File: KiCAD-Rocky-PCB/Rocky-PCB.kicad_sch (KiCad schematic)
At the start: 0 parts

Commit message: Schematic and Sym lib
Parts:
- added BT1: 3.7V Li-Po, symbol Device:Battery_Cell
- added SW1: PWR SW, symbol Switch:SW_SPST
- added U1: ESP32 S3 Sence, symbol Rocky:ESP32-S3-Sence
- added U2: BMP390, symbol Rocky:BMP390
- added U3: GY-91, symbol Rocky:GY-91
- added U4: LC76G, symbol Rocky:LC76G
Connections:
- new net: SW1.2 (B), U1.15 (B+)
- new net: BT1.2 (-), U1.16 (B-)
- new net: BT1.1 (+), SW1.1 (A)
- new net +3.3V: U1.12 (3V3), U2.1 (VCC), U4.1 (VCC)
- new net GND: U1.13 (GND), U2.2 (GND), U3.2 (GND), U4.2 (GND)
- new net I2C-SCL: U1.6 (D5/SCL), U2.4 (SCL), U3.4 (SCL)
- new net I2C-SDA: U1.5 (D4/SDA), U2.3 (SDA), U3.3 (SDA)
- new net uC-Rx: U1.8 (D7/Rx), U4.3 (Tx)
- new net uC-Tx: U1.7 (D6/Tx), U4.4 (Rx)
- no-connect marks 0 -> 7

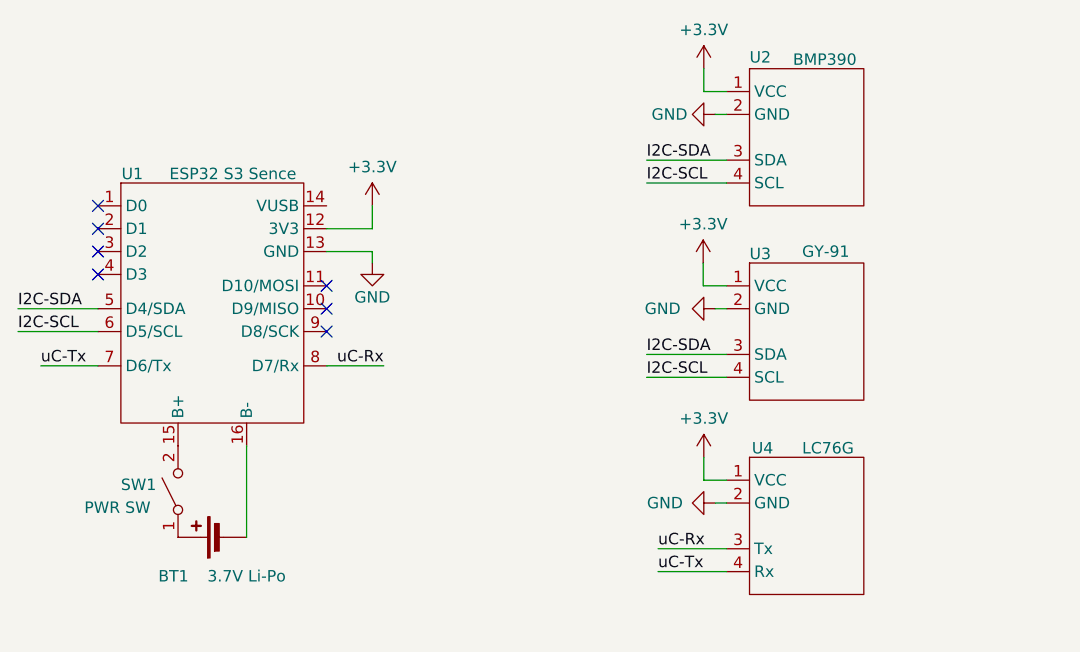
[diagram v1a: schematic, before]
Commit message: Added filtering capacitor and fixed some errors
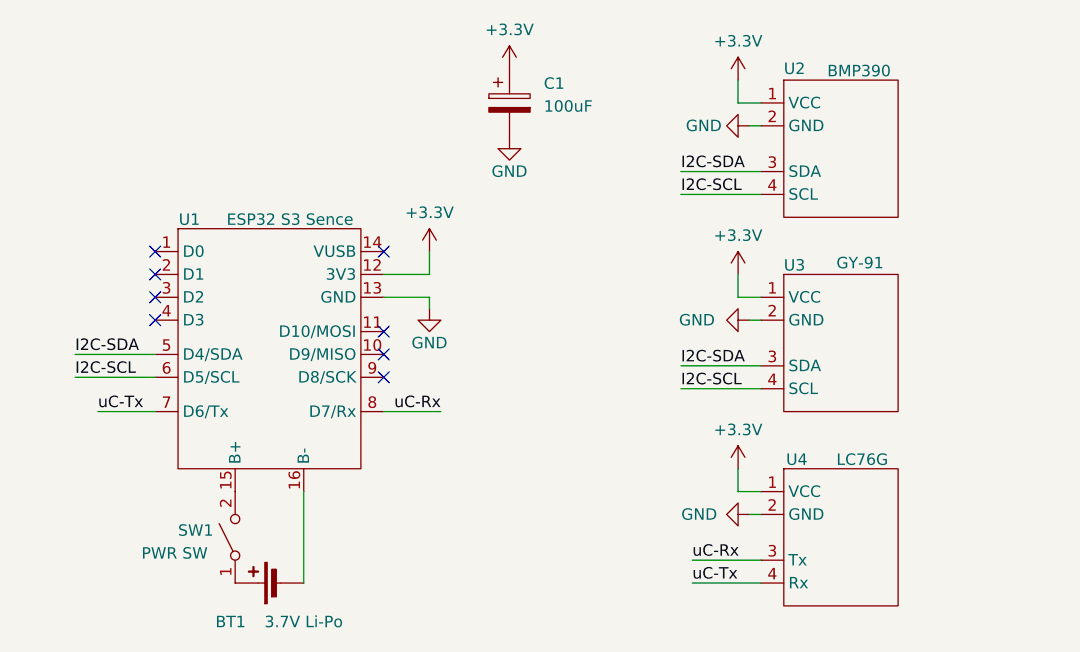
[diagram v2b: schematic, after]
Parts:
- added C1: 100uF, symbol Device:C_Polarized
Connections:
- net +3.3V: now also U3.1 (VCC), C1.1
- net GND: now also C1.2
- no-connect marks 7 -> 8
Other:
- moved on the sheet: BT1, SW1, U1, U2, U3, U4

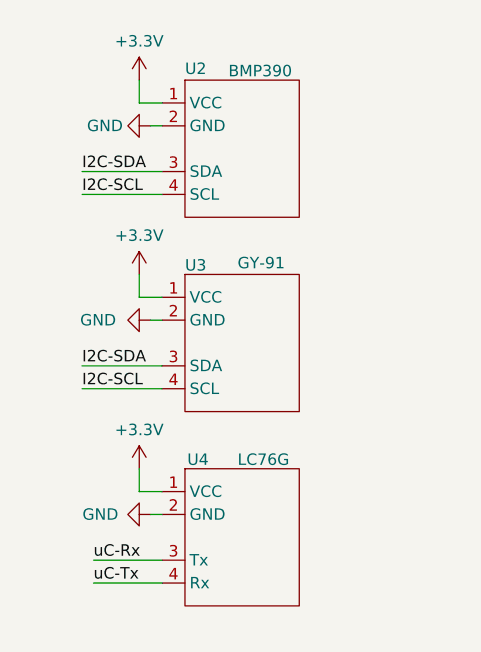
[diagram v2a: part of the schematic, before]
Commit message: Added new filtering capacitors and added a picture of the schematic
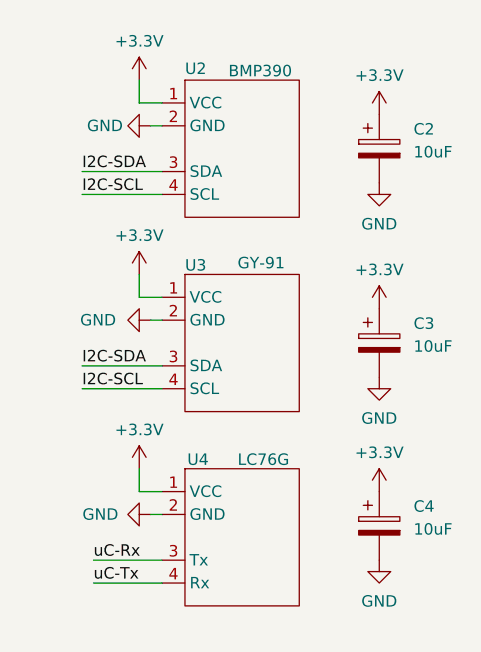
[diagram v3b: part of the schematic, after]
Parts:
- added C2, C3, C4: 10uF, symbol Device:C_Polarized
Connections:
- net +3.3V: now also C2.1, C3.1, C4.1
- net GND: now also C2.2, C3.2, C4.2

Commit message: PCB-V1
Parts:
- BT1: footprint (none) -> Connector_JST:JST_XH_B2B-XH-AM_1x02_P2.50mm_Vertical
- C1: footprint (none) -> Capacitor_THT:CP_Radial_Tantal_D5.5mm_P2.50mm
- C2, C3, C4: footprint (none) -> Capacitor_THT:CP_Radial_Tantal_D4.5mm_P2.50mm
- SW1: footprint (none) -> Rocky-Footprints:DIP4-SW
- U1: footprint (none) -> Rocky-Footprints:XIAO-ESP32-S3-Sence
- U2, U3, U4: footprint (none) -> Connector_JST:JST_XH_B4B-XH-A_1x04_P2.50mm_Vertical
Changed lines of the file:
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@@
 			)
 		)
-		(property "Footprint" ""
+		(property "Footprint" "Rocky-Footprints:XIAO-ESP32-S3-Sence"
 			(at 116.84 105.41 0)
 			(effects
@@
 			)
 		)
-		(property "Footprint" ""
+		(property "Footprint" "Capacitor_THT:CP_Radial_Tantal_D4.5mm_P2.50mm"
 			(at 196.5452 87.63 0)
 			(effects
@@
 			)
 		)
-		(property "Footprint" ""
+		(property "Footprint" "Capacitor_THT:CP_Radial_Tantal_D4.5mm_P2.50mm"
 			(at 196.5452 109.22 0)
 			(effects
@@
 			)
 		)
-		(property "Footprint" ""
+		(property "Footprint" "Connector_JST:JST_XH_B2B-XH-AM_1x02_P2.50mm_Vertical"
 			(at 116.586 132.08 90)
 			(effects
@@
 			)
 		)
-		(property "Footprint" ""
+		(property "Footprint" "Capacitor_THT:CP_Radial_Tantal_D4.5mm_P2.50mm"
 			(at 196.5452 129.54 0)
 			(effects
@@
 			)
 		)
-		(property "Footprint" ""
+		(property "Footprint" "Rocky-Footprints:DIP4-SW"
 			(at 113.03 127 0)
 			(effects
@@
 			)
 		)
-		(property "Footprint" ""
+		(property "Footprint" "Connector_JST:JST_XH_B4B-XH-A_1x04_P2.50mm_Vertical"
 			(at 180.34 127 0)
 			(effects
@@
 			)
 		)
-		(property "Footprint" ""
+		(property "Footprint" "Connector_JST:JST_XH_B4B-XH-A_1x04_P2.50mm_Vertical"
 			(at 180.34 83.82 0)
 			(effects
@@
 			)
 		)
-		(property "Footprint" ""
+		(property "Footprint" "Capacitor_THT:CP_Radial_Tantal_D5.5mm_P2.50mm"
 			(at 144.4752 82.55 0)
 			(effects
@@
 			)
 		)
-		(property "Footprint" ""
+		(property "Footprint" "Connector_JST:JST_XH_B4B-XH-A_1x04_P2.50mm_Vertical"
 			(at 180.34 105.41 0)
 			(effects
